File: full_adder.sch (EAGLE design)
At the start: 24 parts, among them IC1 SN74LS74AN, IC2 NE555, IC3 CD4052BE, IC4 CD4052BE, IC5 CD4052BE, IC6 74HC4051N,652

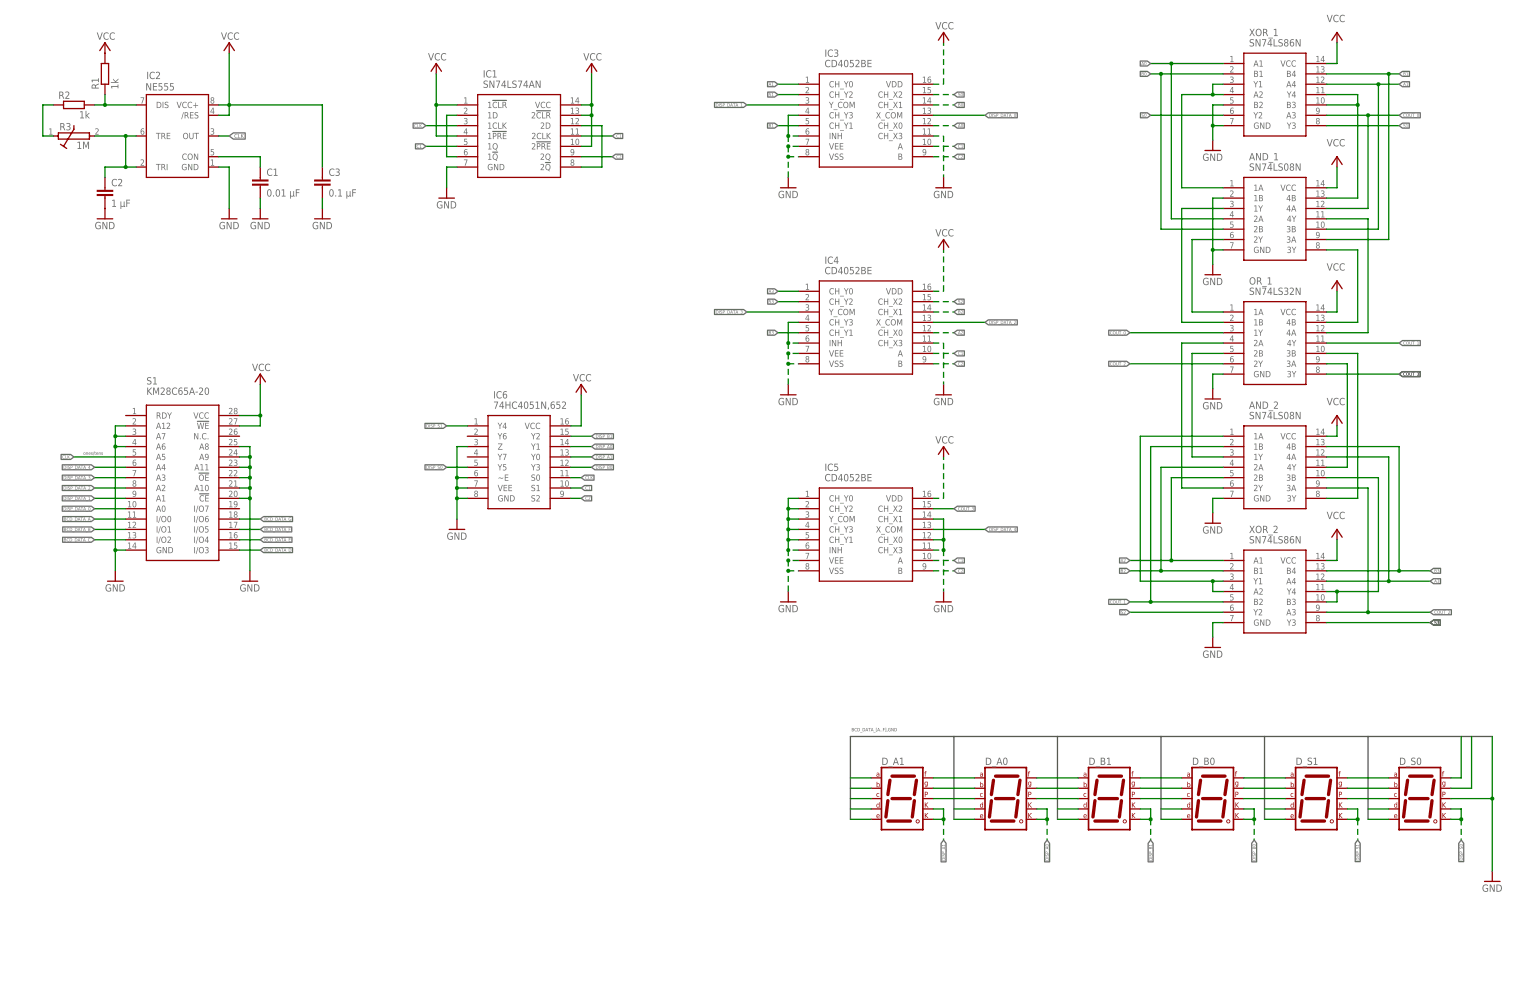
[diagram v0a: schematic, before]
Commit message: binary inputs and outputs added
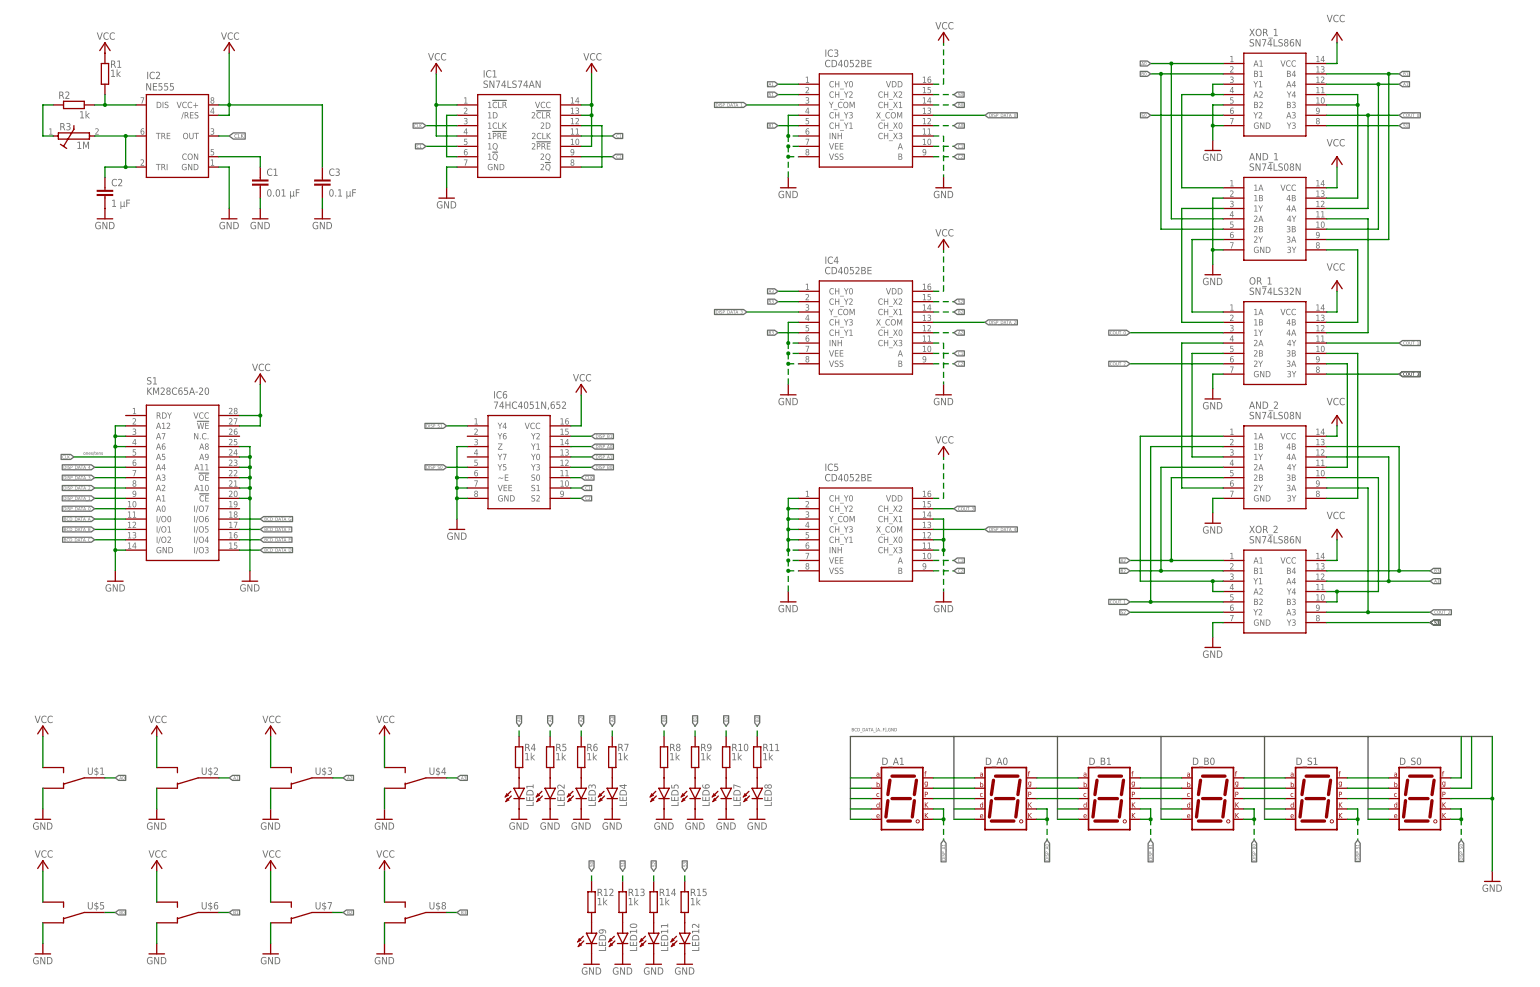
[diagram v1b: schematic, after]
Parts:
- added LED1, LED10, LED11, LED12, LED2, LED3, LED4, LED5, LED6, LED7, LED8, LED9: (no value), led:LED5MM
- added R10, R11, R12, R13, R14, R15, R4, R5, R6, R7, R8, R9: 1k, rcl:R-EU_R1206
- added U$1, U$2, U$3, U$4, U$5, U$6, U$7, U$8: TOGGLESWITCH, custom:TOGGLESWITCH
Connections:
- new net N$18: LED1.A, R4.1
- new net N$19: LED2.A, R5.1
- new net N$20: LED3.A, R6.1
- new net N$21: LED4.A, R7.1
- new net N$22: LED5.A, R8.1
- new net N$23: LED6.A, R9.1
- new net N$24: LED7.A, R10.1
- new net N$25: LED8.A, R11.1
- new net N$26: LED9.A, R12.1
- new net N$27: LED10.A, R13.1
- new net N$28: LED11.A, R14.1
- new net N$29: LED12.A, R15.1
- net A0: now also R4.2, U$1.P$X
- net A1: now also R5.2, U$2.P$X
- net A2: now also R6.2, U$3.P$X
- net A3: now also R7.2, U$4.P$X
- net B0: now also R8.2, U$5.P$X
- net B1: now also R9.2, U$6.P$X
- net B2: now also R10.2, U$7.P$X
- net B3: now also R11.2, U$8.P$X
- net GND: now also LED1.C, LED10.C, LED11.C, LED12.C, LED2.C, LED3.C, LED4.C, LED5.C, LED6.C, LED7.C, LED8.C, LED9.C, U$1.P$A, U$2.P$A, U$3.P$A, U$4.P$A, U$5.P$A, U$6.P$A, U$7.P$A, U$8.P$A
- net S0: now also R12.2
- net S1: now also R13.2
- net S2: now also R14.2
- net S3: now also R15.2
- net VCC: now also U$1.P$B, U$2.P$B, U$3.P$B, U$4.P$B, U$5.P$B, U$6.P$B, U$7.P$B, U$8.P$B
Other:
- note added: "4 Adder"
- note added: "5 EEPROM (bcd decoder)"
- note added: "6 output MUX"
- note added: "7 input selection"
- note added: "8 binary outputs"
- note added: "9 7-segment displays"
- note removed: "4 EEPROM (bcd decoder)"
- note removed: "5 output MUX"
- note removed: "6 7-segment displays"
- note removed: "7 Adder"

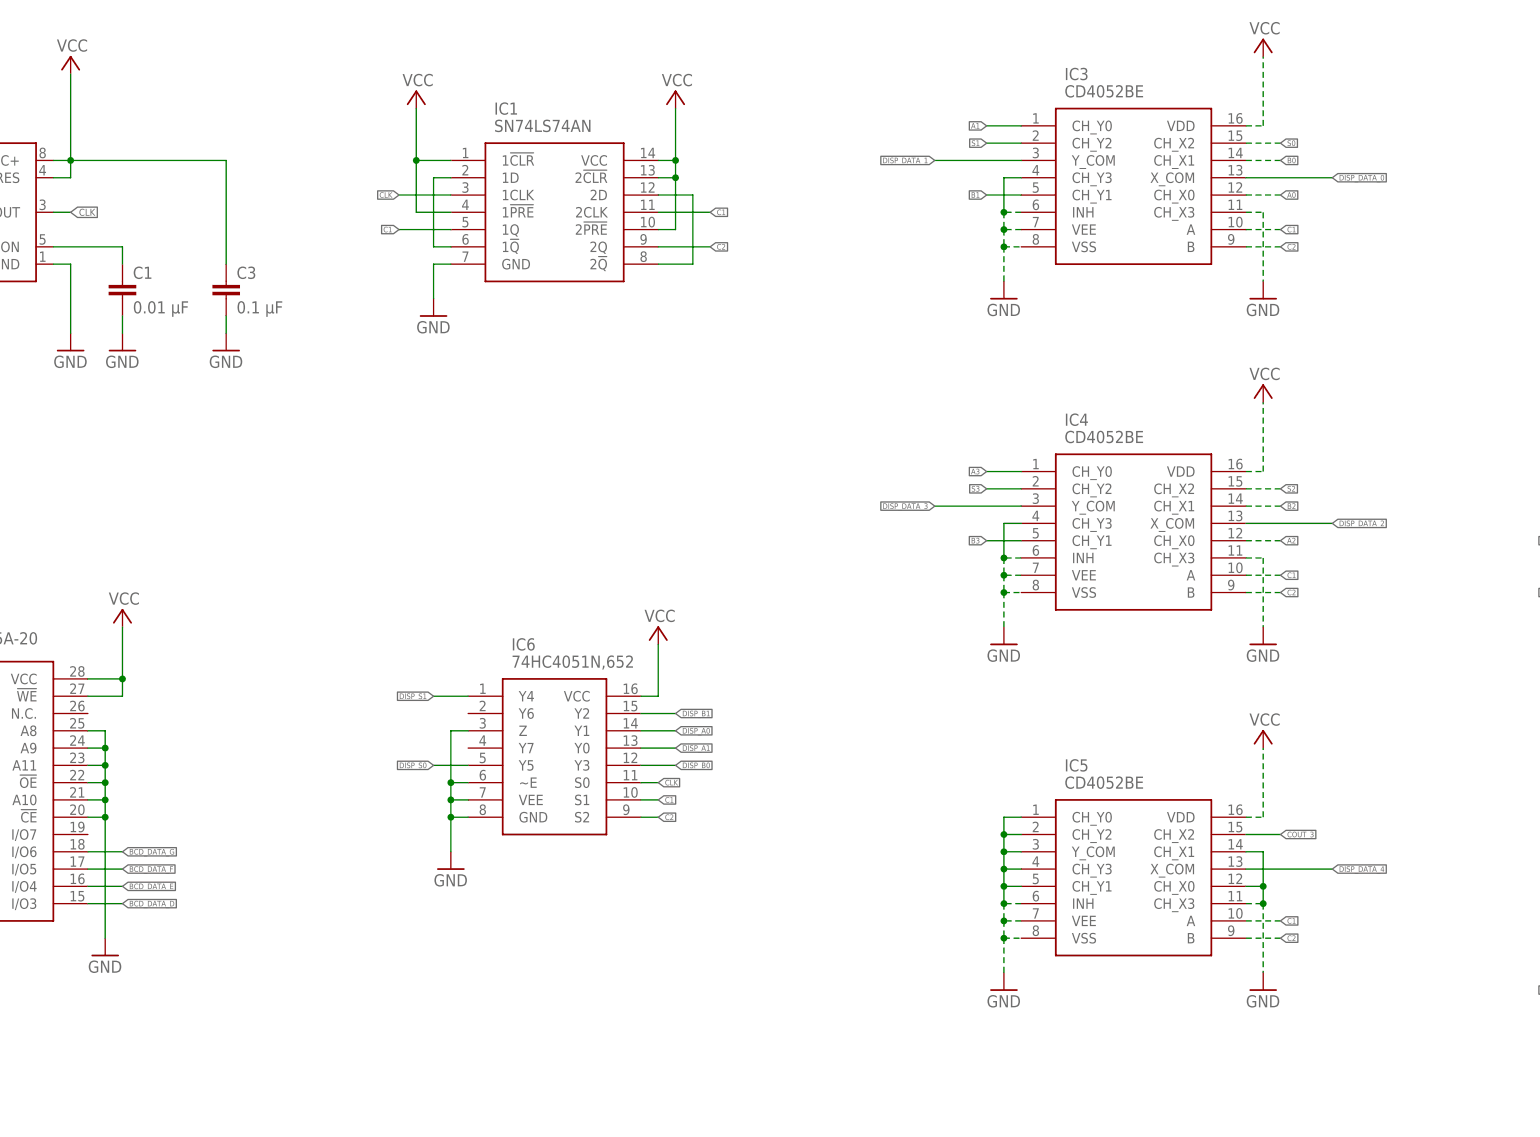
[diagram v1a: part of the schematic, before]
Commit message: added support capacitors
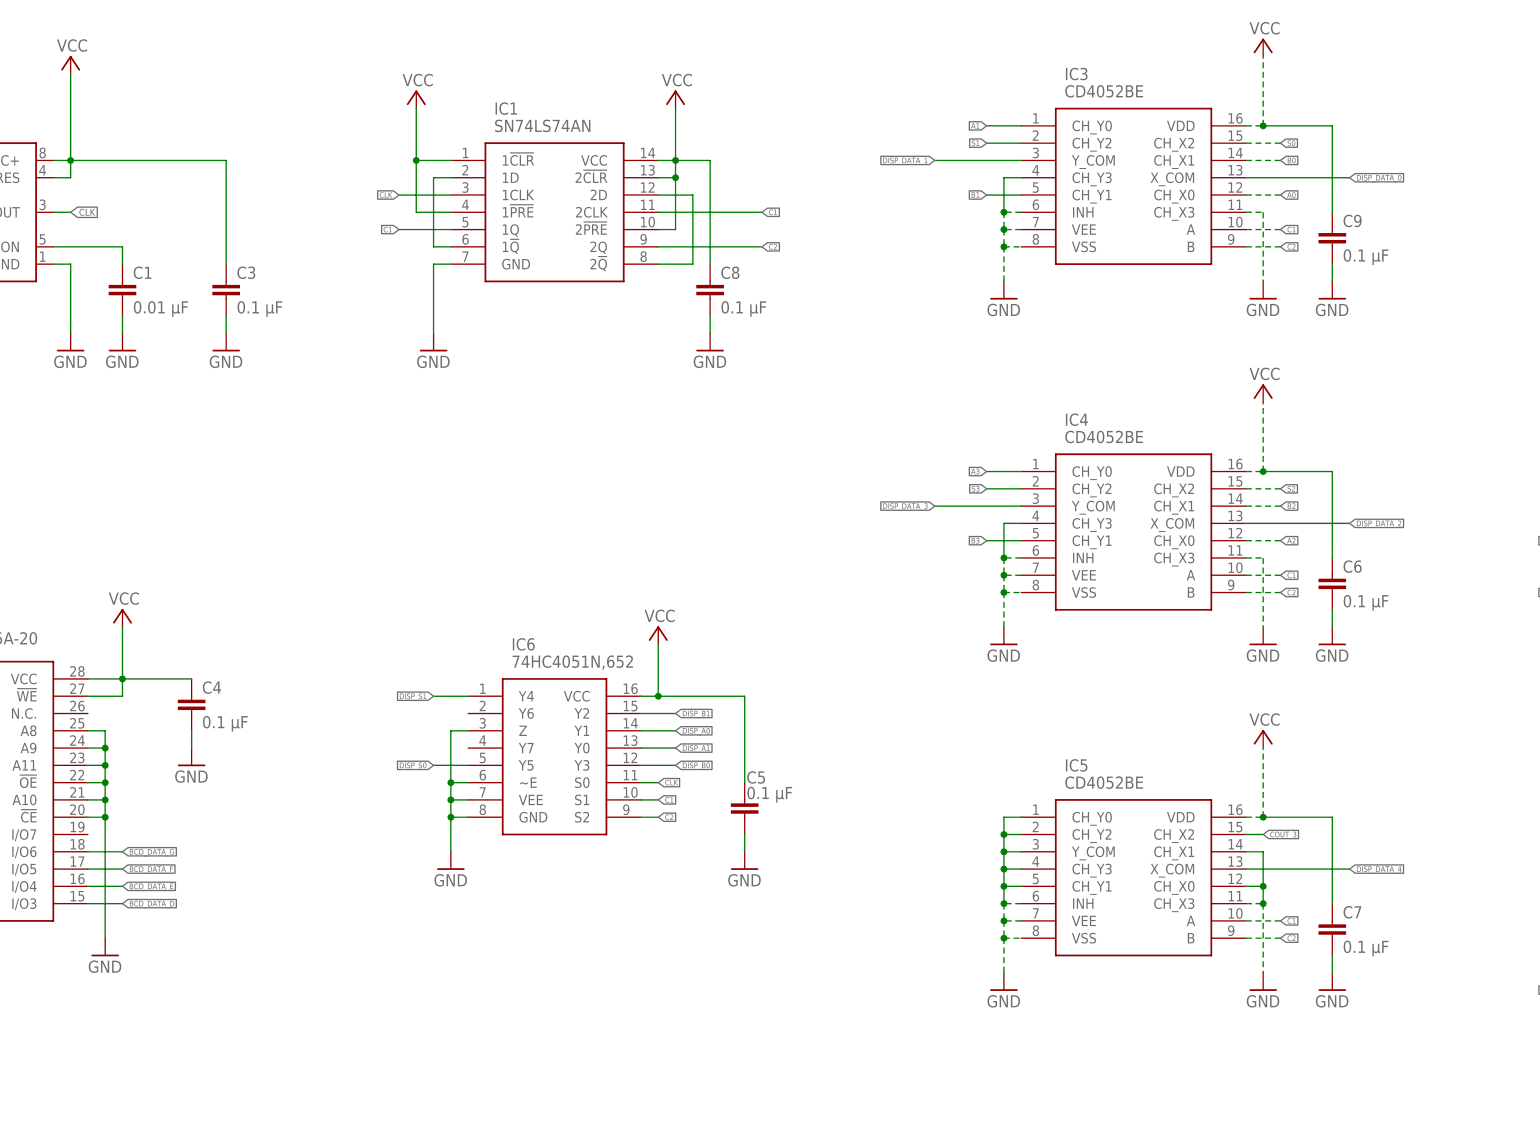
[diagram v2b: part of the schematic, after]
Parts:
- added C4, C5, C6, C7, C8, C9: 0.1 µF, rcl:C-EU025-024X044
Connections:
- net GND: now also C4.2, C5.2, C6.2, C7.2, C8.2, C9.2
- net VCC: now also C4.1, C5.1, C6.1, C7.1, C8.1, C9.1

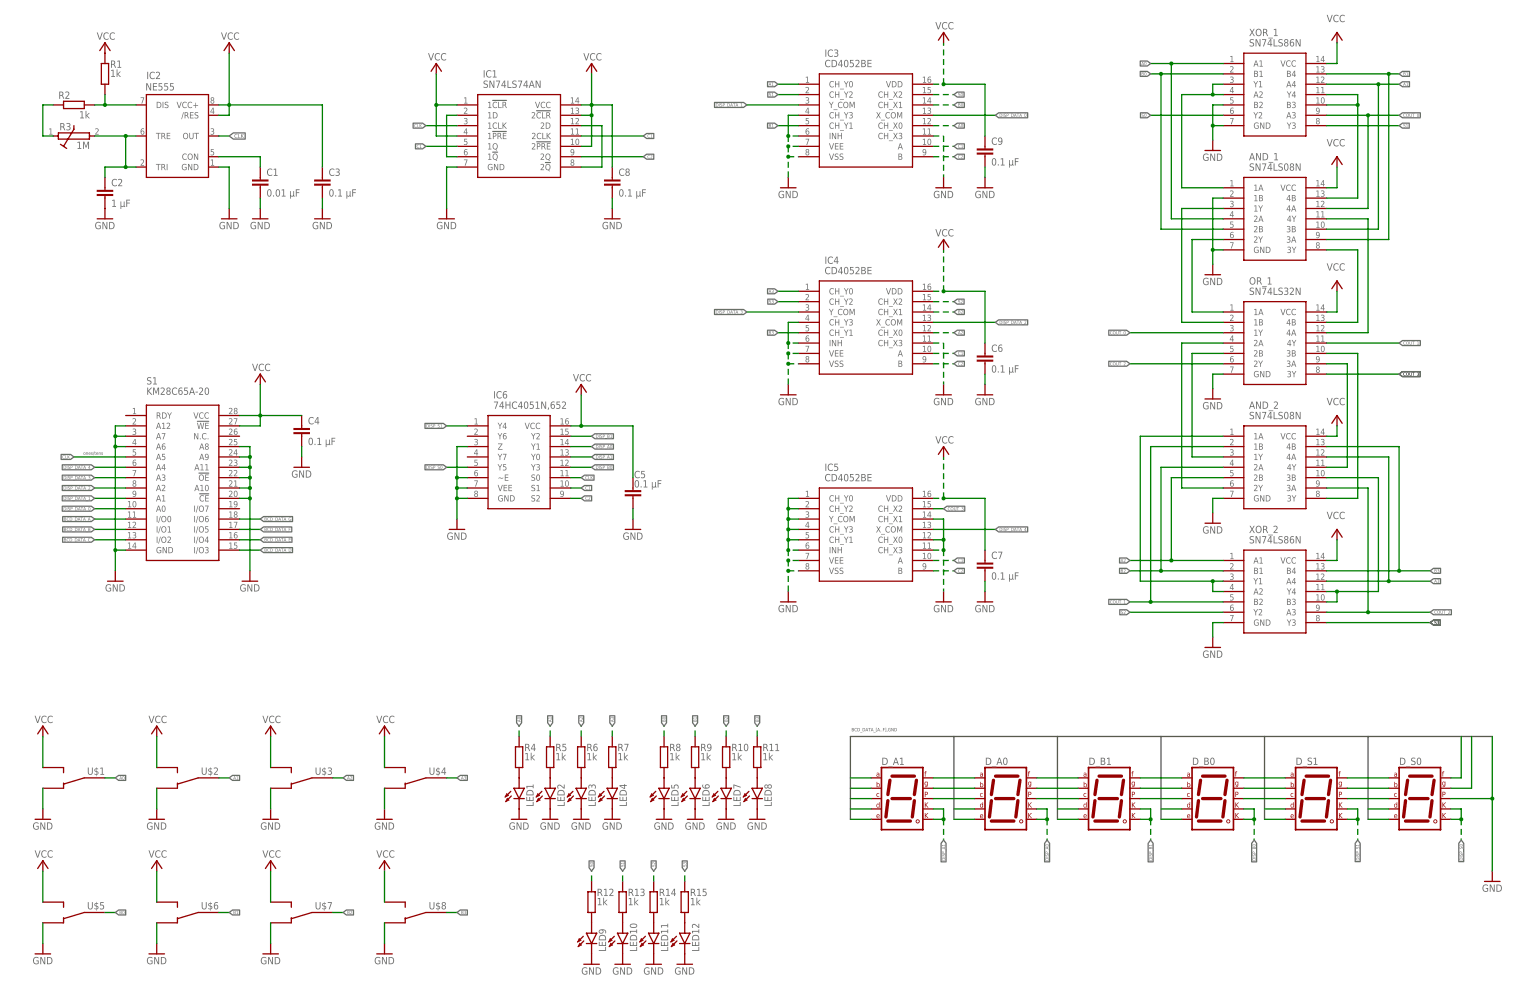
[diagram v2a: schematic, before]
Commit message: Added EEPROM resistors
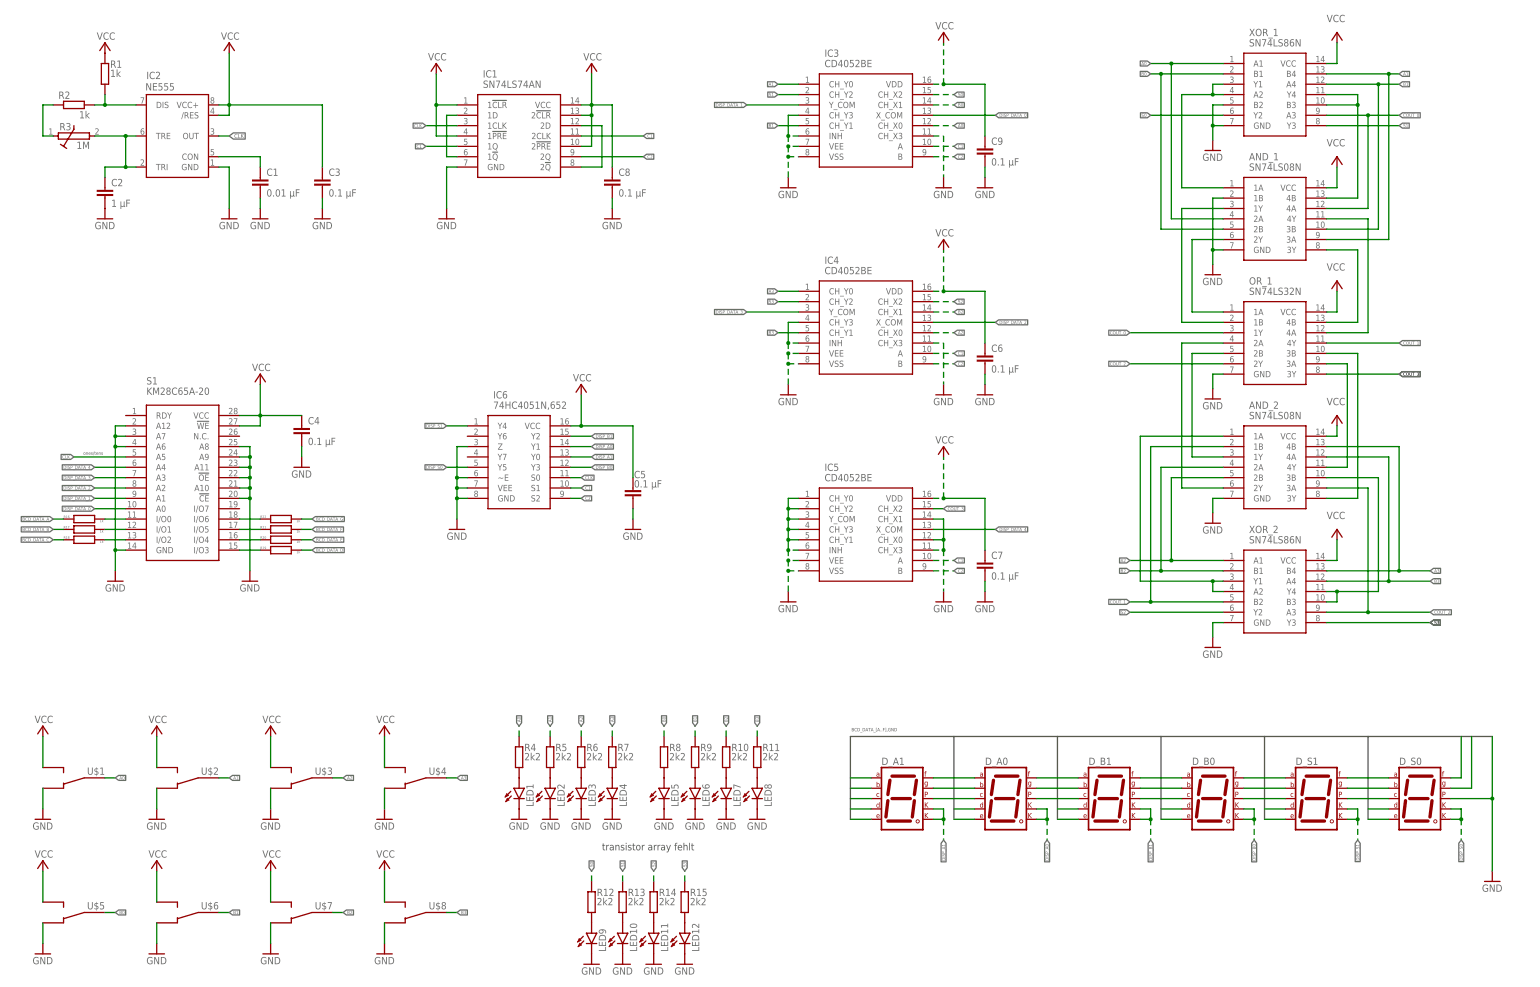
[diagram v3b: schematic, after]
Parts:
- added R16, R17, R18, R19, R20, R21, R22: 1k, rcl:R-EU_R1206
- R10, R11, R12, R13, R14, R15, R4, R5, R6, R7, R8, R9: value 1k -> 2k2
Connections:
- net A1: now also AND_1.3A, XOR_1.B4; no longer AND_1.3B, XOR_1.A4
- net A3: now also AND_2.4B, XOR_2.B4; no longer AND_2.4A, XOR_2.A4
- net B1: now also AND_1.3B, XOR_1.A4; no longer AND_1.3A, XOR_1.B4
- net B3: now also AND_2.4A, XOR_2.A4; no longer AND_2.4B, XOR_2.B4
- net BCD_DATA_A: now also R16.1, R16.2
- net BCD_DATA_B: now also R17.1, R17.2
- net BCD_DATA_C: now also R18.1, R18.2
- net BCD_DATA_D: now also R19.1, R19.2
- net BCD_DATA_E: now also R20.1, R20.2
- net BCD_DATA_F: now also R21.1, R21.2
- net BCD_DATA_G: now also R22.1, R22.2
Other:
- note added: "transistor array fehlt"
